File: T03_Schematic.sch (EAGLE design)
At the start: 26 parts, among them U2 ATMEGA328P_PDIP

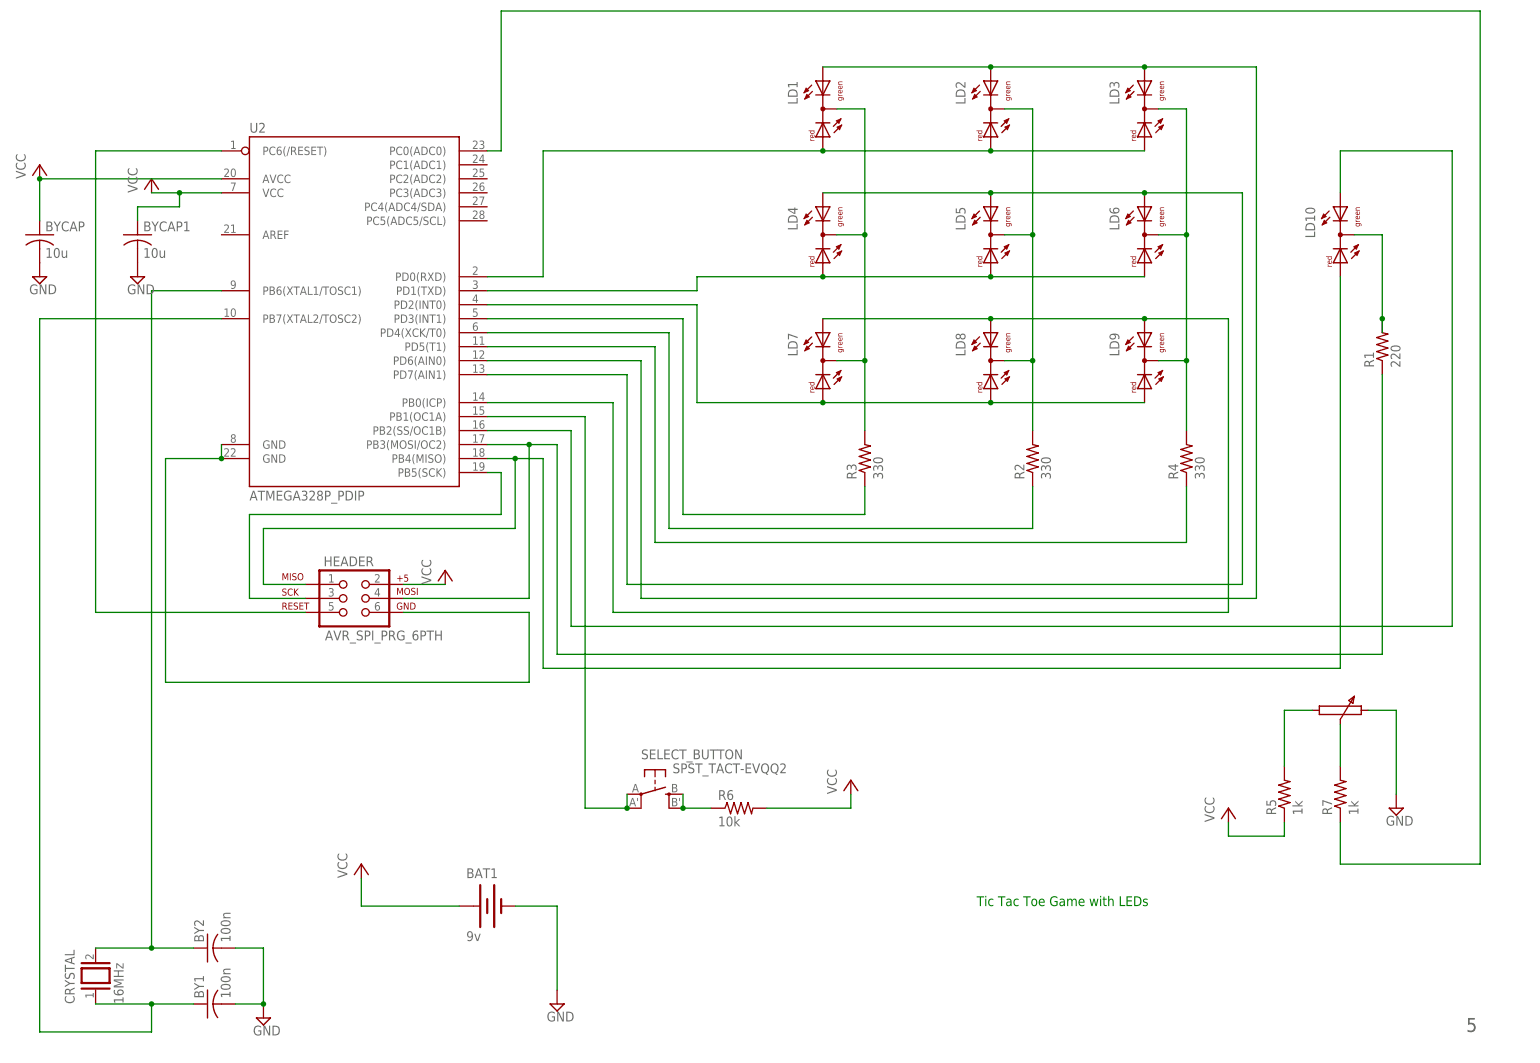
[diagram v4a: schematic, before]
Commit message: Input pins and voltage regulator added. Rev 6
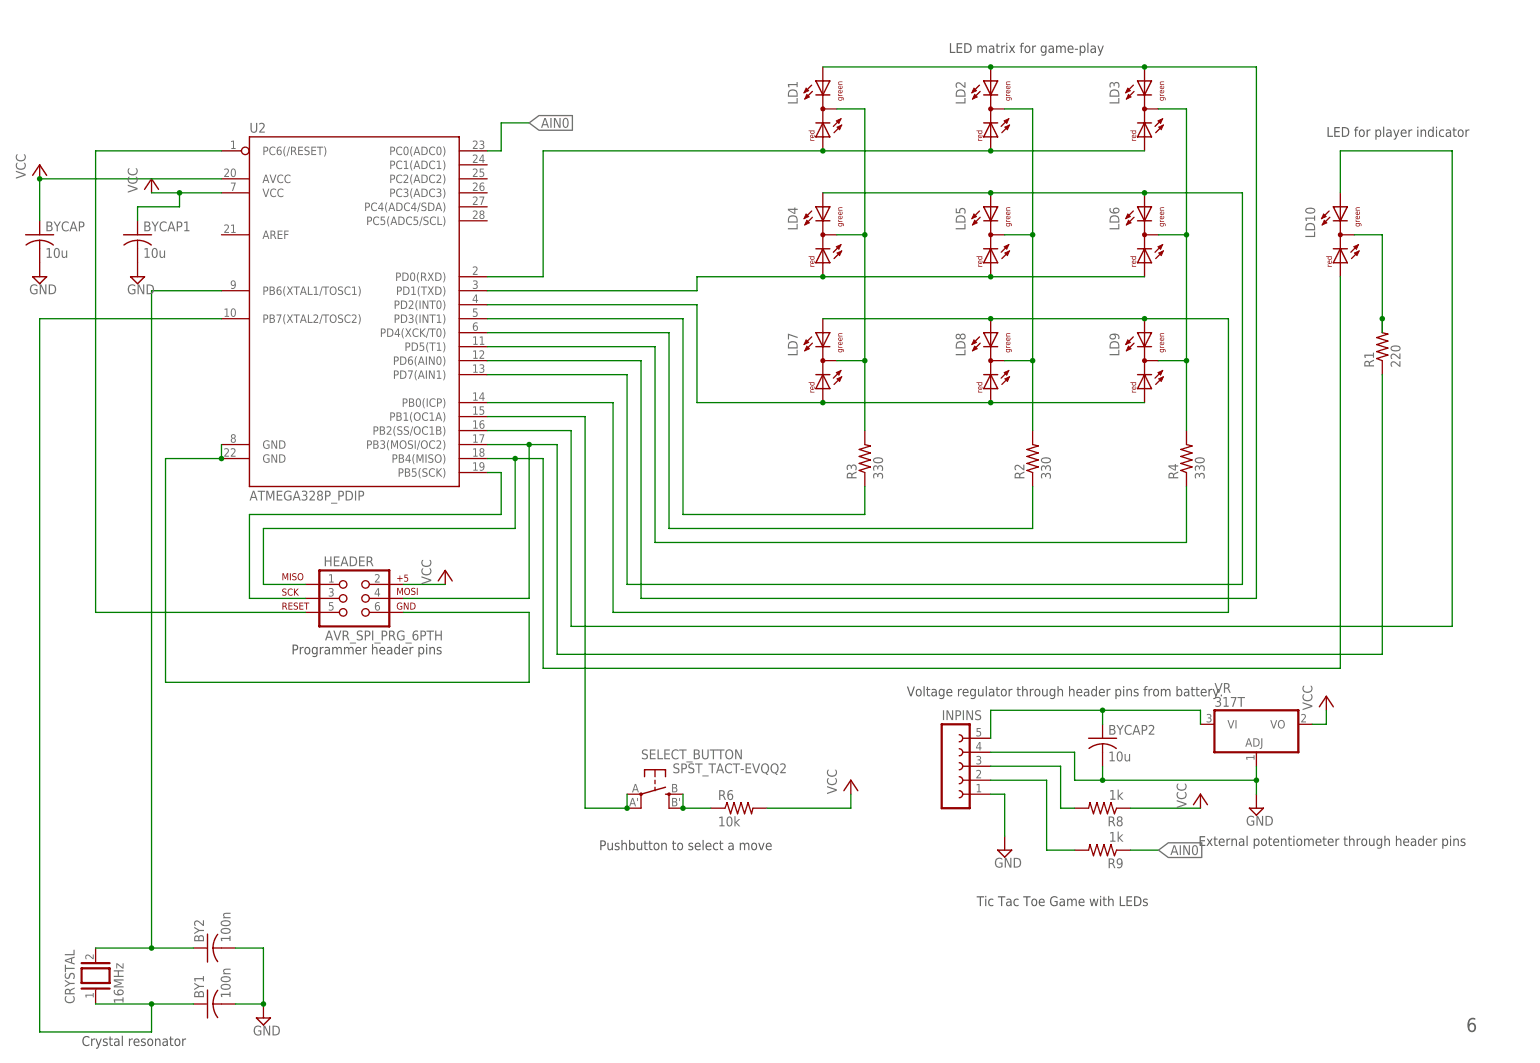
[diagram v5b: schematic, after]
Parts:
- removed BAT1: 9v, SparkFun-Electromechanical:BATTERY9V
- removed R5, R7: 1k, adafruit:R-US_M0805
- added BYCAP2: 10u, adafruit:C-USC0805
- added INPINS: (no value), con-lsta:FE05-1
- added R8, R9: 1k, adafruit:R-US_M0805
- added VR: 317T, linear:317T
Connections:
- removed net CONTROL: R7.1, U2.PC0(ADC0)
- removed net N$4: R5.2
- removed net N$5: R7.2
- new net AIN0: R9.1, U2.PC0(ADC0)
- new net SELECTPIN: INPINS.2, R9.2
- new net V+POT: INPINS.3, R8.2
- new net VIN: BYCAP2.1, INPINS.5, VR.VI
- net GND: now also BYCAP2.2, INPINS.1, INPINS.4, VR.ADJ; no longer BAT1.-
- net VCC: now also R8.1, VR.VO; no longer BAT1.+, R5.1
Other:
- note added: "6"
- note added: "Crystal resonator"
- note added: "External potentiometer through header pins"
- note added: "LED for player indicator"
- note added: "LED matrix for game-play"
- note added: "Programmer header pins"
- note added: "Pushbutton to select a move"
- note added: "Voltage regulator through header pins from battery."
- note removed: "5"

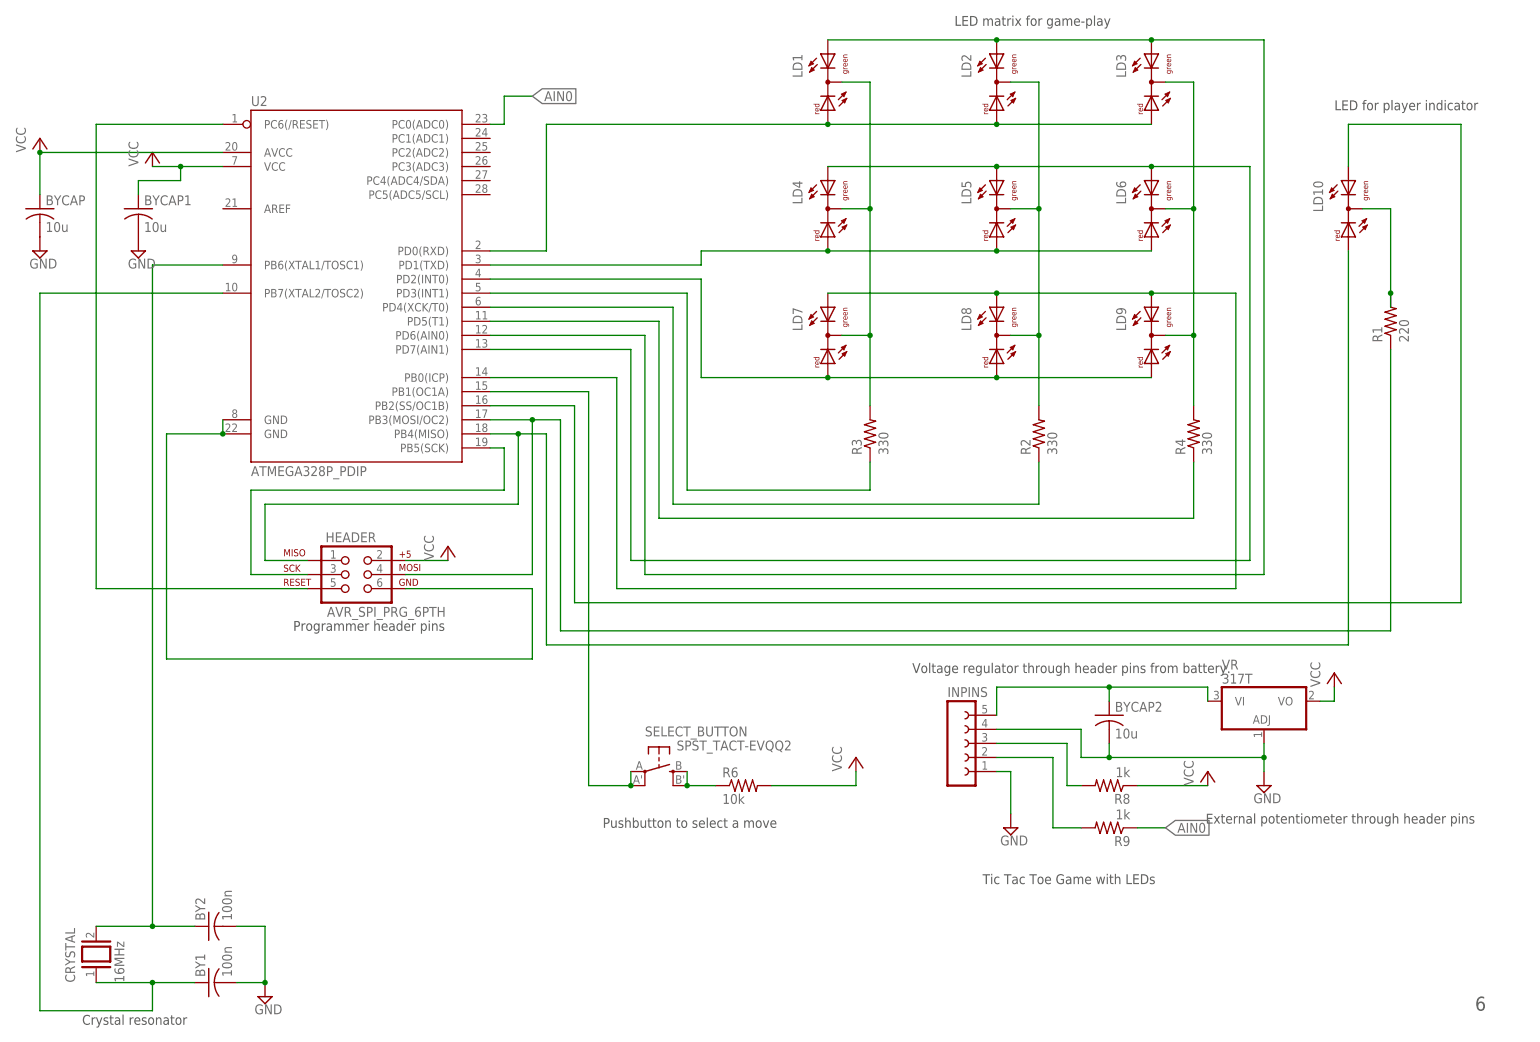
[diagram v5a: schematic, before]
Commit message: Test points added to schematic, board created
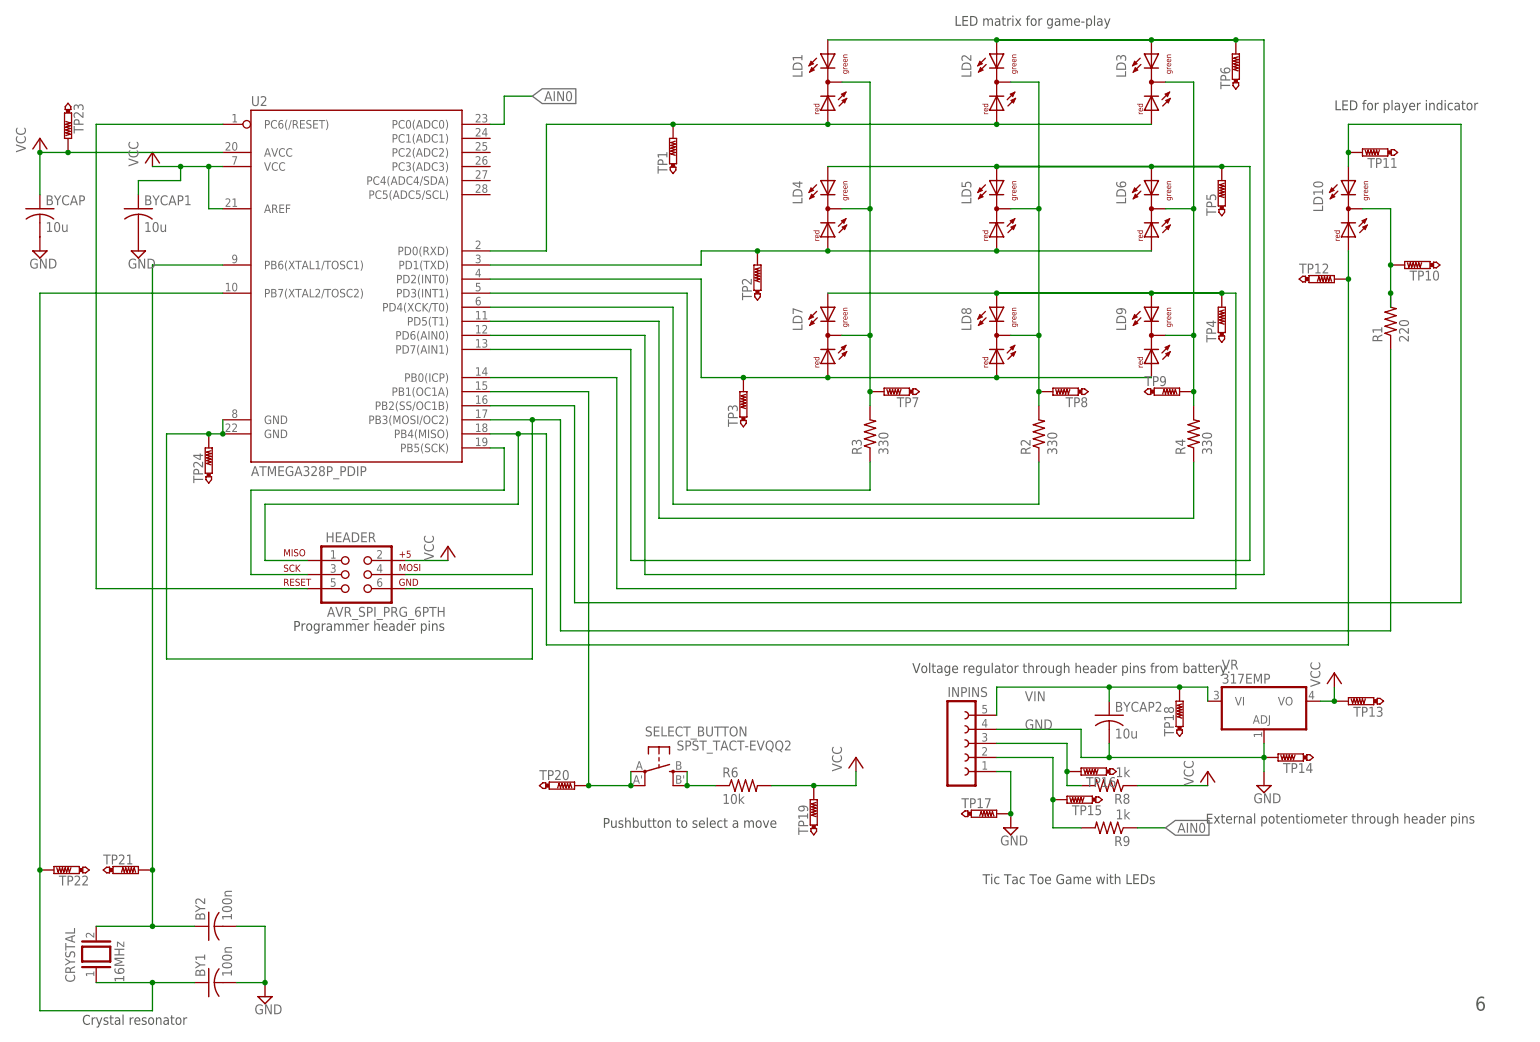
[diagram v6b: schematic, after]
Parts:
- added TP1, TP10, TP11, TP12, TP13, TP14, TP15, TP16, TP17, TP18, TP19, TP2, TP20, TP21, TP22, TP23, TP24, TP3, TP4, TP5, TP6, TP7, TP8, TP9: PTR1B1,27, testpad:PTR1B1,27
- VR: value 317T -> 317EMP; device linear:317T -> linear:317EMP
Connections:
- net GND: now also TP14.TP, TP17.TP
- net GREN1: now also TP6.TP
- net GREN2: now also TP5.TP
- net GREN3: now also TP4.TP
- net N$1: now also TP7.TP
- net N$10: now also TP10.TP
- net N$13: now also TP22.TP
- net N$3: now also TP8.TP
- net N$6: now also TP9.TP
- net N$8: now also TP24.TP
- net PLAY1: now also TP11.TP
- net PLAY2: now also TP12.TP
- net RED1: now also TP1.TP
- net RED2: now also TP2.TP
- net RED3: now also TP3.TP
- net SELECT: now also TP20.TP
- net SELECTPIN: now also TP15.TP
- net V+POT: now also TP16.TP
- net VCC: now also TP13.TP, TP19.TP, TP23.TP, U2.AREF
- net VIN: now also TP18.TP
- net XTAL1: now also TP21.TP

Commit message: Schematic has usb, new board
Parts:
- removed HEADER: AVR_SPI_PRG_6PTH, SparkFun-Connectors:AVR_SPI_PRG_6PTH
- added BYCAP3, BYCAP4: 10u, adafruit:C-USC0805
- added CAP, CAP1: 0.1u, adafruit:C-USC0805
- added IC1: FT230XS, ftdichip:FT230XS
- added R5: 10k, adafruit:R-US_M0805
- added TP25, TP26, TP27: PTR1B1,27, testpad:PTR1B1,27
- added X1: (no value), con-berg:PN61729
- BY1, BY2: value 100n -> 10p
- BYCAP, BYCAP1: value 10u -> 0.1u
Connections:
- net N$13 renamed CRYSTAL-XTAL2
- net XTAL1 renamed CRYSTAL-XTAL1
- removed net N$11: HEADER.3, U2.PB5(SCK)
- removed net N$12: HEADER.5, U2.PC6(/RESET)
- removed net RED1: LD1.AR, LD2.AR, LD3.AR, TP1.TP, U2.PD0(RXD)
- removed net RED2: LD4.AR, LD5.AR, LD6.AR, TP2.TP, U2.PD1(TXD)
- new net N$4: CAP.1, IC1.!RTS
- new net N$5: IC1.USBDP, X1.1
- new net N$7: IC1.USBDM, X1.2
- new net RTS: CAP.2, R5.1, U2.PC6(/RESET)
- new net RXD: IC1.TXD, LD1.AR, LD2.AR, LD3.AR, TP1.TP, U2.PD0(RXD)
- new net TXD: IC1.RXD, LD4.AR, LD5.AR, LD6.AR, TP2.TP, U2.PD1(TXD)
- new net USBVCC: BYCAP3.1, IC1.VCC, TP25.TP, X1.3
- net CATH4: no longer HEADER.4
- net GND: now also BYCAP3.2, BYCAP4.2, CAP1.2, IC1.GND, IC1.GND@1, SELECT_BUTTON.P, SELECT_BUTTON.P1, TP20.TP, TP24.TP, TP26.TP, TP27.TP, U2.GND@1, U2.GND@2, X1.4
- net N$2: no longer SELECT_BUTTON.S
- net N$8: now also CAP1.1, IC1.!RESET; no longer HEADER.6, TP24.TP, U2.GND@1, U2.GND@2
- net PLAY2: no longer HEADER.1
- net SELECT: now also SELECT_BUTTON.S; no longer SELECT_BUTTON.P, SELECT_BUTTON.P1, TP20.TP
- net VCC: now also BYCAP4.1, IC1.VCCIO, R5.2; no longer HEADER.2
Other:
- note added: "7"
- note added: "This is a crystal resonator to act as a clock for the microcontroller."
- note added: "This is a push button that will select a players move location."
- note added: "This is the USB to Serial converter to allow programming the microcontroller via the Arduino IDE and writing via a USB connection."
- note added: "This is the microcontroller, the LED matrix for gameplay, and an LED to indicate the player."
- note added: "This system consists of a set of female header pins for the battery and potentiometer to plug into. The battery pins are then ran through a linear voltage regulator to power the board. The potentiometer is used to select a move location."
- note removed: "6"
- note removed: "Crystal resonator"
- note removed: "External potentiometer through header pins"
- note removed: "Programmer header pins"
- note removed: "Pushbutton to select a move"
- note removed: "Voltage regulator through header pins from battery."
- moved on the sheet: BY1, BY2, BYCAP, BYCAP1, BYCAP2, CRYSTAL, INPINS, LD1, LD10, LD2, LD3, LD4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

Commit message: final layout and schematic
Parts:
- removed SELECT_BUTTON: SPST_TACT-EVQQ2, adafruit:SPST_TACT-EVQQ2
- removed TP21, TP22: PTR1B1,27, testpad:PTR1B1,27
- added S1: DTS-6, switch-tact:DTS-6
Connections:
- net N$7 renamed D-
- removed net N$5: IC1.USBDP, X1.1
- new net D+: IC1.USBDP, X1.3
- new net N$9: BYCAP1.1, U2.AREF
- net CRYSTAL-XTAL1: no longer TP21.TP
- net CRYSTAL-XTAL2: no longer TP22.TP
- net GND: now also S1.1, S1.2; no longer SELECT_BUTTON.P, SELECT_BUTTON.P1
- net N$2: now also S1.4; no longer SELECT_BUTTON.S1
- net SELECT: now also S1.3; no longer SELECT_BUTTON.S
- net USBVCC: now also X1.1; no longer X1.3
- net VCC: no longer BYCAP1.1, U2.AREF
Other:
- moved on the sheet: BYCAP1, CAP1
